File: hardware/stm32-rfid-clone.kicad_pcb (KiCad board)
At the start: 2 copper layers, 0 parts

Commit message: first move
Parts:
- added BT101: BATTERY, stm32:KEYSTONE-3000, F.Cu at (108.4, 53.9)
- added C101: 0.1uF, stm32:CAPC2012X100N, F.Cu at (170.7, 94.7)
- added C102: 48pF, stm32:CAPC2012X100N, F.Cu at (135.6, 112.6)
- added C103: 0.1uF, stm32:CAPC2012X100N, F.Cu at (171.0, 86.6)
- added C104: 48pF, stm32:CAPC2012X100N, F.Cu at (125.4, 114.2)
- added C105: 0.1uF, stm32:CAPC2012X100N, F.Cu at (170.1, 90.1)
- added C106: 0.1uF, stm32:CAPC2012X100N, F.Cu at (175.0, 92.0)
- added C107: 0.1uF, stm32:CAPC2012X100N, F.Cu at (151.9, 86.9)
- added C108: 18pF, stm32:CAPC2012X100N, F.Cu at (137.7, 89.5)
- added C109: 0.1uF, stm32:CAPC2012X100N, F.Cu at (169.6, 97.0)
- added C110: 18pF, stm32:CAPC2012X100N, F.Cu at (150.6, 97.7)
- added C111: 10uF, stm32:CAPC2012X100N, F.Cu at (190.8, 103.7)
- added C112: 10uF, stm32:CAPC2012X100N, F.Cu at (212.0, 50.7)
- added C113: 0.1uF, stm32:CAPC2012X100N, F.Cu at (212.5, 44.9)
- added C114: 0.1uF, stm32:CAPC2012X100N, F.Cu at (198.6, 51.9)
- added C115: 6.8nF, stm32:CAPC2012X100N, F.Cu at (217.0, 47.9)
- added C116: 10uF, stm32:CAPC2012X100N, F.Cu at (216.4, 59.4)
- added C117: 10uF, stm32:CAPC2012X100N, F.Cu at (190.9, 91.6)
- added C118: 10uF, stm32:CAPC2012X100N, F.Cu at (203.9, 87.6)
- added C119: 18pF, stm32:CAPC2012X100N, F.Cu at (160.6, 79.2)
- added C120: 18pF, stm32:CAPC2012X100N, F.Cu at (170.4, 79.3)
- added C201: 6.5-30pF, stm32:MURATA-TZC3, F.Cu at (81.0, 55.0)
- added C202: 1000pF, stm32:CAPC2012X100N, F.Cu at (81.0, 59.0)
- added C203: 2200pF, stm32:CAPC2012X100N, F.Cu at (85.2, 88.5)
- added C204: 1000pF, stm32:CAPC2012X100N, F.Cu at (105.7, 98.8)
- added C205: 1000pF, stm32:CAPC2012X100N, F.Cu at (111.2, 103.6)
- added C206: 1000pF, stm32:CAPC2012X100N, F.Cu at (104.8, 108.3)
- added C207: 1000pF, stm32:CAPC2012X100N, F.Cu at (90.6, 94.7)
- added C208: 1000pF, stm32:CAPC2012X100N, F.Cu at (87.1, 105.7)
- added C209: 1000pF, stm32:CAPC2012X100N, F.Cu at (105.5, 88.5)
- added C210: 1000pF, stm32:CAPC2012X100N, F.Cu at (100.6, 85.2)
- added D101: DIODESCH, stm32:DIOM5226X220N, F.Cu at (216.1, 84.9)
- added D102: DIODESCH, stm32:DIOM5226X220N, F.Cu at (135.2, 105.7)
- added D104: PWR, stm32:LEDC3216X100N, F.Cu at (173.2, 101.2)
- added D105: DIODESCH, stm32:DIOM5226X220N, F.Cu at (162.6, 60.4)
- added D106: DIODESCH, stm32:DIOM5226X220N, F.Cu at (194.6, 80.0)
- added D201: DIODE, stm32:DIOM5226X220N, F.Cu at (84.6, 65.4)
- added D202: DIODE, stm32:DIOM5226X220N, F.Cu at (85.0, 73.8)
- added D203: DIODE, stm32:DIOM5226X220N, F.Cu at (79.0, 65.0)
- added J101: USB, stm32:JST_UB-MC5BR3-SD204-4S-NMP, F.Cu at (135.6, 119.2)
- added L101: 27uH, stm32:IND_ASPI-8040S-680M-T, F.Cu at (206.7, 57.9)
- added L102: 27uH, stm32:IND_ASPI-8040S-680M-T, F.Cu at (200.7, 96.0)
- added M101: Mouting Hole, stm32:MTGNP565H328Z565P, F.Cu at (168.5, 117.9)
- added M102: Mouting Hole, stm32:MTGNP565H328Z565P, F.Cu at (176.6, 50.6)
- added M103: Mouting Hole, stm32:MTGNP565H328Z565P, F.Cu at (78.6, 116.7)
- added M104: Mouting Hole, stm32:MTGNP565H328Z565P, F.Cu at (73.9, 51.5)
- added P101: JTAG10, stm32:SHDRV10W66P254_2X5_2035X870X609P, F.Cu at (126.0, 55.2)
- added P102: BATTERY, stm32:HDRV2W66P254_1X2_508X249X838P, F.Cu at (220.3, 87.2)
- added P103: DEBUG, stm32:HDRV3W66P254_1X3_762X249X838P, F.Cu at (128.6, 67.3)
- added P104: READIND, stm32:HDRV3W66P254_1X3_762X249X838P, F.Cu at (150.0, 50.4)
- added P105: SPEAKER, stm32:HDRV2W66P254_1X2_508X249X838P, F.Cu at (162.0, 53.5)
- added P201: ANT, stm32:HDRV2W66P254_1X2_508X249X838P, F.Cu at (84.8, 50.4)
- added Q201: 2N2222, stm32:SOT95P237X112_123-3N, F.Cu at (96.9, 69.3)
- added Q202: 2N2222, stm32:SOT95P237X112_123-3N, F.Cu at (92.1, 65.0)
- added Q203: 2N2907, stm32:SOT95P237X112_123-3N, F.Cu at (97.0, 65.0)
- added R101: 22R, stm32:RESC2012X100N, F.Cu at (124.9, 109.9)
- added R102: 22R, stm32:RESC2012X100N, F.Cu at (124.6, 118.4)
- added R103: 10K, stm32:RESC2012X100N, F.Cu at (128.0, 105.7)
- added R104: 1.5K, stm32:RESC2012X100N, F.Cu at (141.3, 113.6)
- added R105: 10K, stm32:RESC2012X100N, F.Cu at (158.1, 84.8)
- added R106: 10K, stm32:RESC2012X100N, F.Cu at (101.0, 126.0)
- added R107: 100R, stm32:RESC2012X100N, F.Cu at (153.3, 56.7)
- added R108: 100R, stm32:RESC2012X100N, F.Cu at (147.2, 58.3)
- added R109: 1.5K, stm32:RESC2012X100N, F.Cu at (161.5, 101.8)
- added R110: 100R, stm32:RESC2012X100N, F.Cu at (173.4, 105.5)
- added R111: 100K, stm32:RESC2012X100N, F.Cu at (221.5, 44.6)
- added R112: 6.8K, stm32:RESC2012X100N, F.Cu at (222.0, 51.3)
- added R113: 26.1K, stm32:RESC2012X100N, F.Cu at (216.0, 54.7)
- added R114: 10K, stm32:RESC2012X100N, F.Cu at (224.1, 56.0)
- added R115: ?, stm32:RESC2012X100N, F.Cu at (169.7, 53.3)
- added R116: 31.6K, stm32:RESC2012X100N, F.Cu at (198.7, 86.7)
- added R117: 5K, stm32:RESC2012X100N, F.Cu at (210.4, 96.5)
- added R118: 3.3K, stm32:RESC2012X100N, F.Cu at (130.7, 109.7)
- added R119: 6.8K, stm32:RESC2012X100N, F.Cu at (136.3, 110.3)
- added R201: 1.2K, stm32:RESC2012X100N, F.Cu at (96.8, 72.7)
- added R202: 470R, stm32:RESC2012X100N, F.Cu at (88.1, 64.8)
- added R203: 10R, stm32:RESC2012X100N, F.Cu at (87.0, 57.0)
- added R204: 10R, stm32:RESC2012X100N, F.Cu at (87.0, 54.0)
- added R205: 390K, stm32:RESC2012X100N, F.Cu at (114.6, 98.5)
- added R206: 1M, stm32:RESC2012X100N, F.Cu at (105.5, 95.6)
- added R207: 1.82K, stm32:RESC2012X100N, F.Cu at (110.0, 107.0)
- added R208: 47.5K, stm32:RESC2012X100N, F.Cu at (95.7, 109.3)
- added R209: 2.67K, stm32:RESC2012X100N, F.Cu at (105.3, 104.9)
- added R210: 10M, stm32:RESC2012X100N, F.Cu at (90.2, 91.0)
- added R211: 82.5K, stm32:RESC2012X100N, F.Cu at (90.5, 98.5)
- added R212: 10K, stm32:RESC2012X100N, F.Cu at (91.3, 101.6)
- added R213: 10K, stm32:RESC2012X100N, F.Cu at (105.9, 91.3)
- added R214: 10K, stm32:RESC2012X100N, F.Cu at (97.4, 90.2)
- added R215: 15.5K, stm32:RESC2012X100N, F.Cu at (106.2, 85.4)
- added R216: 10K, stm32:RESC2012X100N, F.Cu at (84.4, 103.3)
- added R217: 500R, stm32:COPAL-CT6EP, F.Cu at (83.9, 97.6)
- added R218: 10K, stm32:RESC2012X100N, F.Cu at (84.6, 91.7)
- added R219: 6.2K, stm32:RESC2012X100N, F.Cu at (115.3, 91.9)
- added R220: 3.6K, stm32:RESC2012X100N, F.Cu at (98.1, 105.9)
- added R221: 1M, stm32:RESC2012X100N, F.Cu at (105.3, 101.7)
- added S101: RESET, stm32:CKCOMP-PTS525SM10SMTR, F.Cu at (148.6, 81.7)
- added S102: WRITEEN, stm32:APEM-MJTP1129B, F.Cu at (93.0, 125.0)
- added S103: POWER, stm32:CKCOMP-OS102011MA1QN1, F.Cu at (151.2, 118.3)
- added TP201: RFTX, stm32:HDRV1W66P254_1X1_254X249X838P, F.Cu at (103.1, 71.3)
- added TP202: RF1, stm32:HDRV1W66P254_1X1_254X249X838P, F.Cu at (110.1, 98.8)
- added TP203: RF2, stm32:HDRV1W66P254_1X1_254X249X838P, F.Cu at (100.0, 109.3)
- added TP204: RF3, stm32:HDRV1W66P254_1X1_254X249X838P, F.Cu at (91.6, 106.0)
- added TP205: RF4, stm32:HDRV1W66P254_1X1_254X249X838P, F.Cu at (101.3, 89.5)
- added TP206: RFRX, stm32:HDRV1W66P254_1X1_254X249X838P, F.Cu at (124.3, 87.5)
- added U101: MOSFET-P, stm32:SOT95P237X112_123-3N, F.Cu at (142.8, 109.0)
- added U102: STM32-48PIN, stm32:QFP50P900X900X160-48N, F.Cu at (161.7, 92.8)
- added U103: AP6502, stm32:SOIC127P600X150-9N, F.Cu at (205.1, 46.6)
- added U104: MOSFET-N, stm32:SOT95P237X112_123-3N, F.Cu at (170.1, 59.1)
- added U105: MIC2288, stm32:SOT95P280X100-5N, F.Cu at (192.3, 85.4)
- added U201: TL084, stm32:SOIC127P600X175-14N, F.Cu at (97.5, 97.5)
- added X101: 8MHz, stm32:XTAL8045X200N, F.Cu at (147.8, 91.9)
- added X102: 32.768kHz, stm32:SOJ550P370X240-4N, F.Cu at (165.5, 79.4)
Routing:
- added copper zone on F.Cu, net GNDPWR

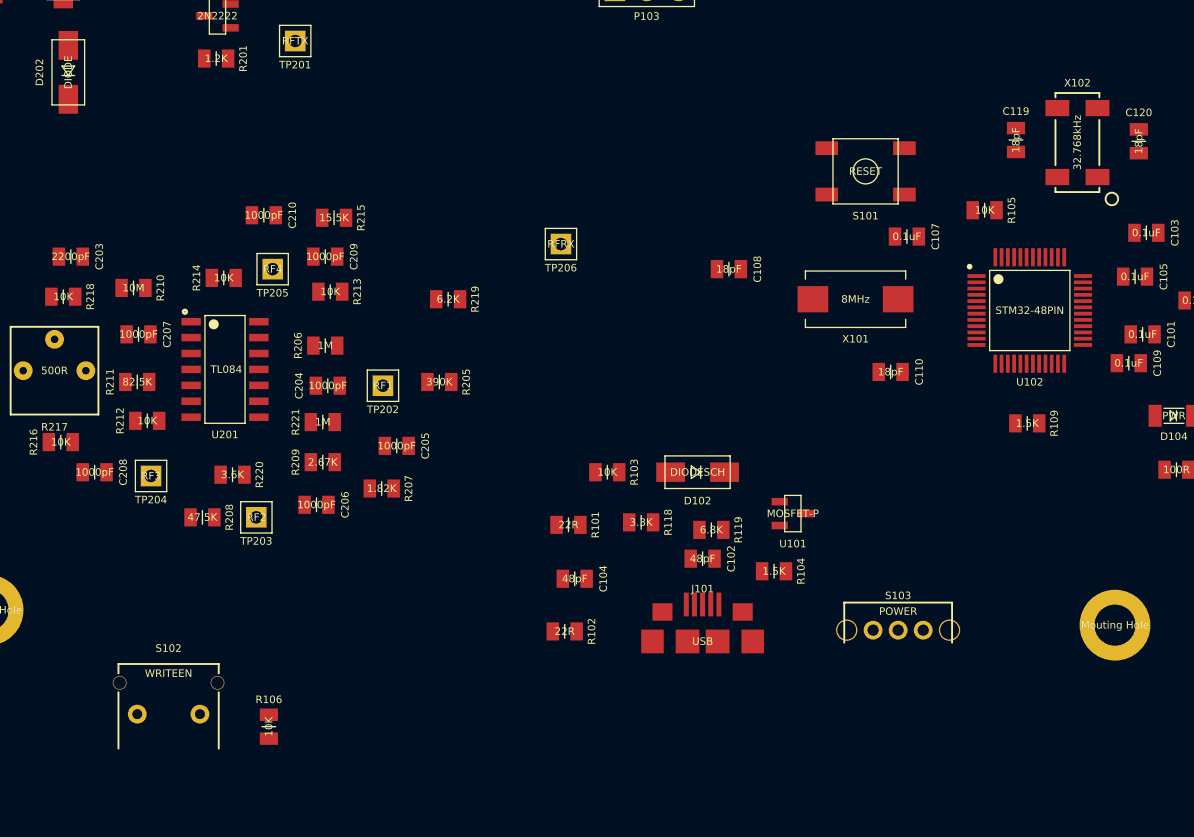
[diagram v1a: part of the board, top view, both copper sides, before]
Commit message: changed mods and libs to better represent pins
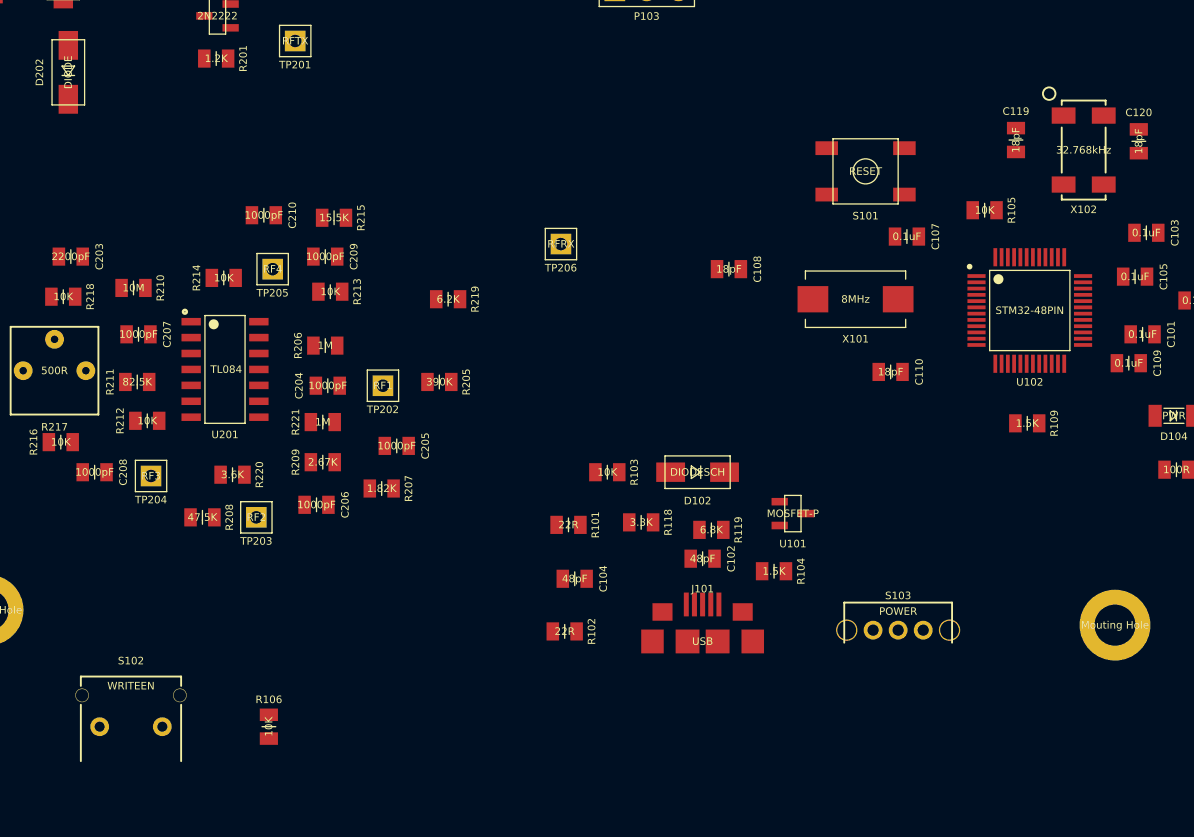
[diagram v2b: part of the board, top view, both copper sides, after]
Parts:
- moved S102 3.16 mm to (90.0, 126.0)
- moved X102 0.78 mm to (166.0, 80.0), turned to 0 degrees
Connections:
- S102 pad 2: +3.3V -> /WRITEEN
- X101 pad 1: Net-(C110-Pad1) -> Net-(C108-Pad1)
- X101 pad 2: Net-(C108-Pad1) -> Net-(C110-Pad1)
- X102 pad 1: Net-(C120-Pad1) -> Net-(C119-Pad1)
- X102 pad 2: Net-(C119-Pad1) -> (no net)
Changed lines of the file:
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@@
     (fp_line (start 4 -2.25) (end 4 -1.6) (layer F.SilkS) (width 0.1))
     (pad 1 smd rect (at -3.4 0) (size 2.45 2.1) (layers F.Cu F.Paste F.Mask)
+      (net 25 "Net-(C108-Pad1)"))
+    (pad 2 smd rect (at 3.4 0) (size 2.45 2.1) (layers F.Cu F.Paste F.Mask)
       (net 26 "Net-(C110-Pad1)"))
-    (pad 2 smd rect (at 3.4 0) (size 2.45 2.1) (layers F.Cu F.Paste F.Mask)
-      (net 25 "Net-(C108-Pad1)"))
-  )
-  (module stm32:SOJ550P370X240-4N (layer F.Cu)
-    (at 165.5 79.4 180)
-    (fp_text reference X102 (at 0 4.75 180) (layer F.SilkS)
-      (effects (font (size 0.6 0.6) (thickness 0.1)))
-    )
-    (fp_text value 32.768kHz (at 0 0 270) (layer F.SilkS)
-      (effects (font (size 0.6 0.6) (thickness 0.1)))
-    )
-    (fp_circle (center -2.75 -4.5) (end -2.25 -4.5) (layer F.SilkS) (width 0.15))
-    (fp_line (start -2.55 -4.2) (end 2.55 -4.2) (layer Cmts.User) (width 0.15))
-    (fp_line (start 2.55 -4.2) (end 2.55 4.2) (layer Cmts.User) (width 0.15))
-    (fp_line (start 2.55 4.2) (end -2.55 4.2) (layer Cmts.User) (width 0.15))
-    (fp_line (start -2.55 4.2) (end -2.55 -4.2) (layer Cmts.User) (width 0.15))
-    (fp_line (start -1.75 -3.6) (end -1.75 -3.95) (layer F.SilkS) (width 0.15))
-    (fp_line (start -1.75 1.8) (end -1.75 -1.8) (layer F.SilkS) (width 0.15))
-    (fp_line (start 1.75 3.95) (end 1.75 3.6) (layer F.SilkS) (width 0.15))
-    (fp_line (start 1.75 3.95) (end -1.75 3.95) (layer F.SilkS) (width 0.15))
-    (fp_line (start -1.75 3.6) (end -1.75 3.95) (layer F.SilkS) (width 0.15))
-    (fp_line (start 1.75 -1.8) (end 1.75 1.8) (layer F.SilkS) (width 0.15))
-    (fp_line (start -1.75 -3.95) (end 1.75 -3.95) (layer F.SilkS) (width 0.15))
-    (fp_line (start 1.75 -3.95) (end 1.75 -3.6) (layer F.SilkS) (width 0.15))
-    (pad 1 smd rect (at -1.6 -2.75 180) (size 1.9 1.3) (layers F.Cu F.Paste F.Mask)
-      (net 33 "Net-(C120-Pad1)"))
-    (pad "" smd rect (at -1.6 2.75 180) (size 1.9 1.3) (layers F.Cu F.Paste F.Mask))
-    (pad "" smd rect (at 1.6 2.75 180) (size 1.9 1.3) (layers F.Cu F.Paste F.Mask))
-    (pad 2 smd rect (at 1.6 -2.75 180) (size 1.9 1.3) (layers F.Cu F.Paste F.Mask)
-      (net 32 "Net-(C119-Pad1)"))
   )
   (module stm32:APEM-MJTP1129B (layer F.Cu)
-    (at 93 125 180)
+    (at 90 126 180)
     (fp_text reference S102 (at 0 5.25 180) (layer F.SilkS)
       (effects (font (size 0.6 0.6) (thickness 0.1)))
@@
     (fp_line (start -1.5 -12.35) (end -1.5 -3.9) (layer Dwgs.User) (width 0.15))
     (fp_line (start -1.5 -12.35) (end 1.5 -12.35) (layer Dwgs.User) (width 0.15))
-    (pad 3 thru_hole circle (at -2.5 0 180) (size 1.5 1.5) (drill 0.8) (layers *.Cu *.Mask F.SilkS)
+    (pad 1 thru_hole circle (at -2.5 0 180) (size 1.5 1.5) (drill 0.8) (layers *.Cu *.Mask F.SilkS)
+      (net 1 +3.3V))
+    (pad 2 thru_hole circle (at 2.5 0 180) (size 1.5 1.5) (drill 0.8) (layers *.Cu *.Mask F.SilkS)
       (net 20 /WRITEEN))
-    (pad 2 thru_hole circle (at 2.5 0 180) (size 1.5 1.5) (drill 0.8) (layers *.Cu *.Mask F.SilkS)
-      (net 1 +3.3V))
     (pad "" thru_hole circle (at -3.9 2.5 180) (size 1.1 1.1) (drill 1) (layers *.Cu *.Mask F.SilkS))
     (pad "" thru_hole circle (at 3.9 2.5 180) (size 1.1 1.1) (drill 1) (layers *.Cu *.Mask F.SilkS))
   )
+  (module stm32:SOJ550P370X240-4N (layer F.Cu)
+    (at 166 80)
+    (fp_text reference X102 (at 0 4.75) (layer F.SilkS)
+      (effects (font (size 0.6 0.6) (thickness 0.1)))
+    )
+    (fp_text value 32.768kHz (at 0 0) (layer F.SilkS)
+      (effects (font (size 0.6 0.6) (thickness 0.1)))
+    )
+    (fp_circle (center -2.75 -4.5) (end -2.25 -4.5) (layer F.SilkS) (width 0.15))
+    (fp_line (start -2.55 -4.2) (end 2.55 -4.2) (layer Cmts.User) (width 0.15))
+    (fp_line (start 2.55 -4.2) (end 2.55 4.2) (layer Cmts.User) (width 0.15))
+    (fp_line (start 2.55 4.2) (end -2.55 4.2) (layer Cmts.User) (width 0.15))
+    (fp_line (start -2.55 4.2) (end -2.55 -4.2) (layer Cmts.User) (width 0.15))
+    (fp_line (start -1.75 -3.6) (end -1.75 -3.95) (layer F.SilkS) (width 0.15))
+    (fp_line (start -1.75 1.8) (end -1.75 -1.8) (layer F.SilkS) (width 0.15))
+    (fp_line (start 1.75 3.95) (end 1.75 3.6) (layer F.SilkS) (width 0.15))
+    (fp_line (start 1.75 3.95) (end -1.75 3.95) (layer F.SilkS) (width 0.15))
+    (fp_line (start -1.75 3.6) (end -1.75 3.95) (layer F.SilkS) (width 0.15))
+    (fp_line (start 1.75 -1.8) (end 1.75 1.8) (layer F.SilkS) (width 0.15))
+    (fp_line (start -1.75 -3.95) (end 1.75 -3.95) (layer F.SilkS) (width 0.15))
+    (fp_line (start 1.75 -3.95) (end 1.75 -3.6) (layer F.SilkS) (width 0.15))
+    (pad 1 smd rect (at -1.6 -2.75) (size 1.9 1.3) (layers F.Cu F.Paste F.Mask)
+      (net 32 "Net-(C119-Pad1)"))
+    (pad 2 smd rect (at -1.6 2.75) (size 1.9 1.3) (layers F.Cu F.Paste F.Mask))
+    (pad 3 smd rect (at 1.6 2.75) (size 1.9 1.3) (layers F.Cu F.Paste F.Mask))
+    (pad 4 smd rect (at 1.6 -2.75) (size 1.9 1.3) (layers F.Cu F.Paste F.Mask)
+      (net 33 "Net-(C120-Pad1)"))
+  )
   (zone (net 22) (net_name GNDPWR) (layer F.Cu) (hatch edge 0.508)

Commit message: pcb layout
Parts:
- moved R112 151.5 mm to (92.0, 129.0), turned to 270 degrees
- moved C115 146.9 mm to (92.0, 125.0), turned to 270 degrees
- moved C113 144.3 mm to (96.0, 130.0)
- moved R111 143.2 mm to (103.0, 125.0), turned to 90 degrees
- moved R114 140.3 mm to (100.0, 121.5)
- moved L101 137.9 mm to (86.5, 125.5), turned to 270 degrees
- moved R113 137.3 mm to (96.0, 121.5)
- moved C116 134.3 mm to (96.0, 119.0)
- moved C112 134.2 mm to (103.0, 129.0), turned to 270 degrees
- moved U103 133.1 mm to (97.9, 125.5), turned to 180 degrees
- moved C114 125.8 mm to (100.0, 130.0)
- moved D101 98.8 mm to (129.5, 132.5), turned to 180 degrees
- moved R117 94.0 mm to (121.0, 125.5), turned to 90 degrees
- moved C118 93.4 mm to (118.5, 125.5), turned to 90 degrees
- moved R116 89.3 mm to (120.0, 129.0), turned to 0 degrees
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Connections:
- net Net-(C102-Pad1) renamed /USBDP
- net Net-(C104-Pad1) renamed /USBDM
- C109 pad 1: +3.3V -> /VBAT
- U102 pad 11: /LEDGRN -> Net-(U102-Pad11)
- U102 pad 12: /LEDRED -> Net-(U102-Pad12)
- U102 pad 13: /BEEP -> /USBDET
- U102 pad 25: Net-(U102-Pad25) -> /LEDGRN
- U102 pad 26: Net-(U102-Pad26) -> /LEDRED
- U102 pad 27: Net-(U102-Pad27) -> /BEEP
- U102 pad 42: /USBDET -> Net-(U102-Pad42)
- U201 pad 10: Net-(C204-Pad2) -> +3.3V
- U201 pad 12: Net-(C209-Pad2) -> Net-(C204-Pad2)
- U201 pad 13: Net-(R214-Pad1) -> Net-(C205-Pad1)
- U201 pad 14: Net-(C210-Pad2) -> Net-(C206-Pad2)
- U201 pad 5: +3.3V -> Net-(C209-Pad2)
- U201 pad 6: Net-(C207-Pad2) -> Net-(R214-Pad1)
- U201 pad 7: Net-(C208-Pad2) -> Net-(C210-Pad2)
- U201 pad 8: Net-(C206-Pad2) -> Net-(C208-Pad2)
- U201 pad 9: Net-(C205-Pad1) -> Net-(C207-Pad2)
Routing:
- net +3.3V: track 0.00 -> 217.4 mm, vias 0 -> 7
- net GNDPWR: track 0.00 -> 67.4 mm, vias 0 -> 27
- net /VIN: track 0.00 -> 59.1 mm, vias 0 -> 3
- net +9V: track 0.00 -> 54.0 mm, vias 0 -> 2
- net /nRST: track 0.00 -> 51.0 mm, vias 0 -> 2
- net /USBDP: track 0.00 -> 45.7 mm, vias 0 -> 2
- net /VBAT: track 0.00 -> 44.7 mm, vias 0 -> 2
- net /WRITEEN: track 0.00 -> 40.4 mm, vias 0 -> 2
- net /USBDM: track 0.00 -> 39.3 mm, vias 0 -> 2
- net /USBDIS: track 0.00 -> 32.5 mm, vias 0 -> 2
- net /RF/RX: track 0.00 -> 31.3 mm, vias 0 -> 2
- net Net-(C210-Pad2): track 0.00 -> 29.1 mm, vias 0 -> 2
- net Net-(C114-Pad2): track 0.00 -> 27.9 mm, vias 0 -> 2
- net /USBDET: track 0.00 -> 27.7 mm, vias 0 -> 2
- net Net-(C210-Pad1): track 0.00 -> 27.6 mm, vias 0 -> 4
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- added copper zone on B.Cu, net GNDPWR
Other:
- net class Default: clearance 0.254 -> 0.2032
- rule trace_clearance: 0.254 -> 0.2032
